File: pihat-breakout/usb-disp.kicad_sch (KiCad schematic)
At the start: 19 parts, among them J8 USB_A, U5 TPS259535DSGT

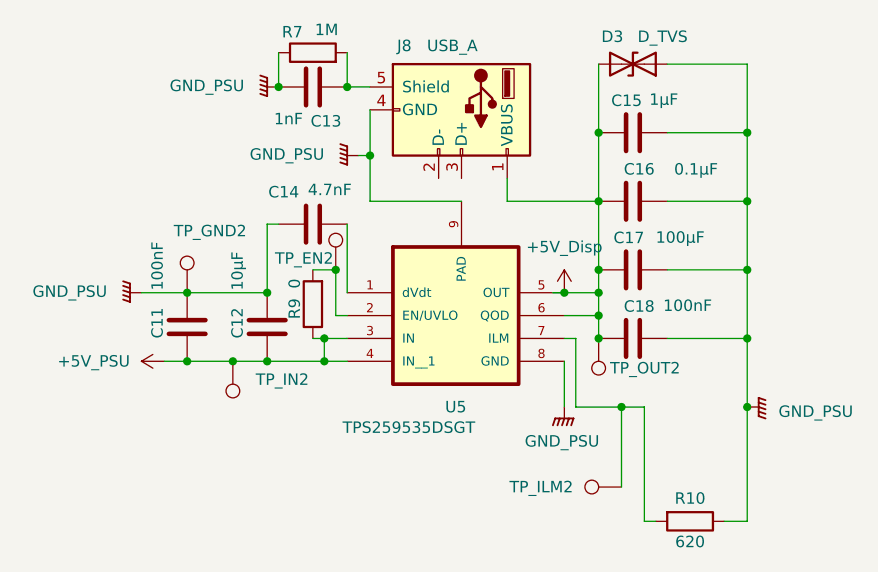
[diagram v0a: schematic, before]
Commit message: fix(0.1uF->100nF)
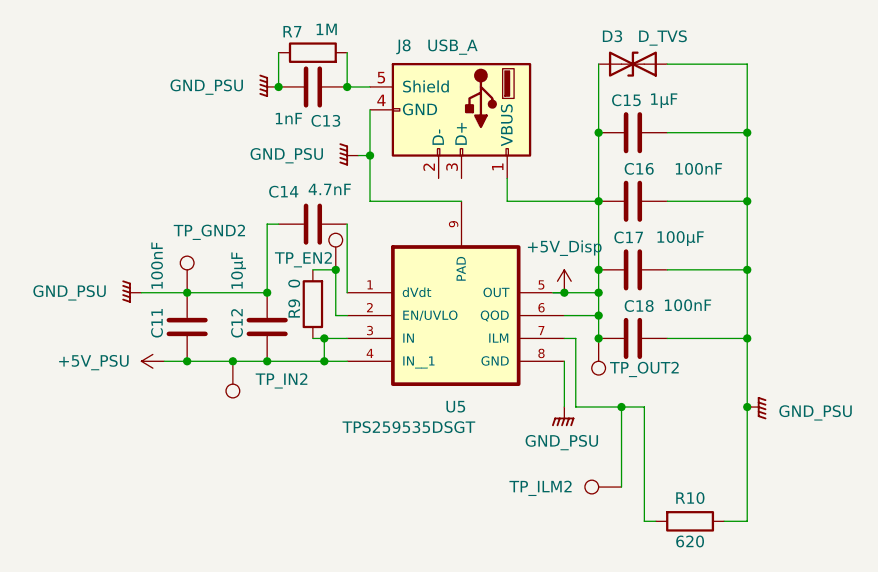
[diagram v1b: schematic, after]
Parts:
- C16: value 0.1µF -> 100nF
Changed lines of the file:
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@@
 			)
 		)
-		(property "Value" "0.1µF"
+		(property "Value" "100nF"
 			(at 162.052 75.184 90)
 			(effects
